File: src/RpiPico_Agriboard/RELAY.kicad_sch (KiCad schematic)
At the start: 7 parts, among them J8 Screw_Terminal_01x03, K2 G5Q-14 DC5, Q10 AP3404

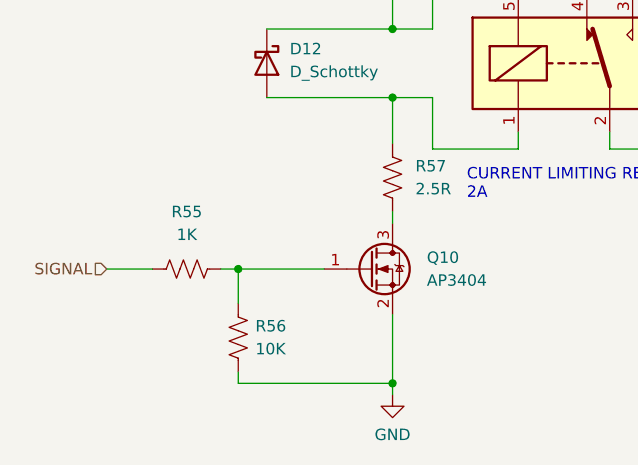
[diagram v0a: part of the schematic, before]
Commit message: power module supply line increase and reupdates on schematic
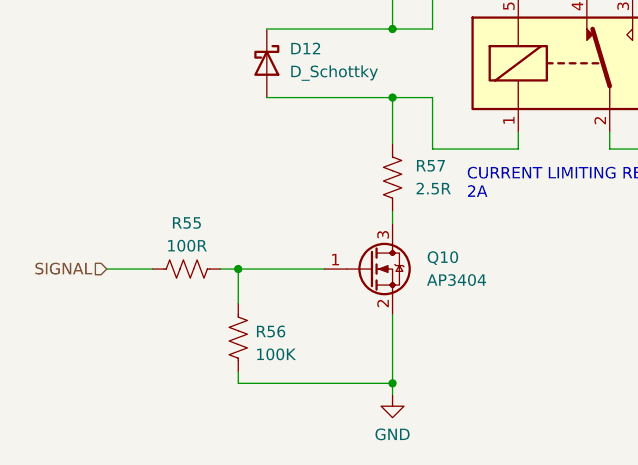
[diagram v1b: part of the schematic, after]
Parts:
- R55: value 1K -> 100R
- R56: value 10K -> 100K
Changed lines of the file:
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@@
   (symbol (lib_id "Device:R_US") (at 97.79 114.3 90) (unit 1)
     (in_bom yes) (on_board yes) (dnp no) (fields_autoplaced)
-    (property "Reference" "R55" (at 97.79 107.95 90)
+    (property "Reference" "R55" (at 97.79 109.22 90)
       (effects (font (size 1.27 1.27)))
     )
-    (property "Value" "1K" (at 97.79 110.49 90)
+    (property "Value" "100R" (at 97.79 111.76 90)
       (effects (font (size 1.27 1.27)))
     )
@@
   (symbol (lib_id "Device:R_US") (at 103.505 121.92 0) (unit 1)
     (in_bom yes) (on_board yes) (dnp no) (fields_autoplaced)
-    (property "Reference" "R56" (at 105.41 120.6499 0)
+    (property "Reference" "R56" (at 105.41 121.285 0)
       (effects (font (size 1.27 1.27)) (justify left))
     )
-    (property "Value" "10K" (at 105.41 123.1899 0)
+    (property "Value" "100K" (at 105.41 123.825 0)
       (effects (font (size 1.27 1.27)) (justify left))
     )

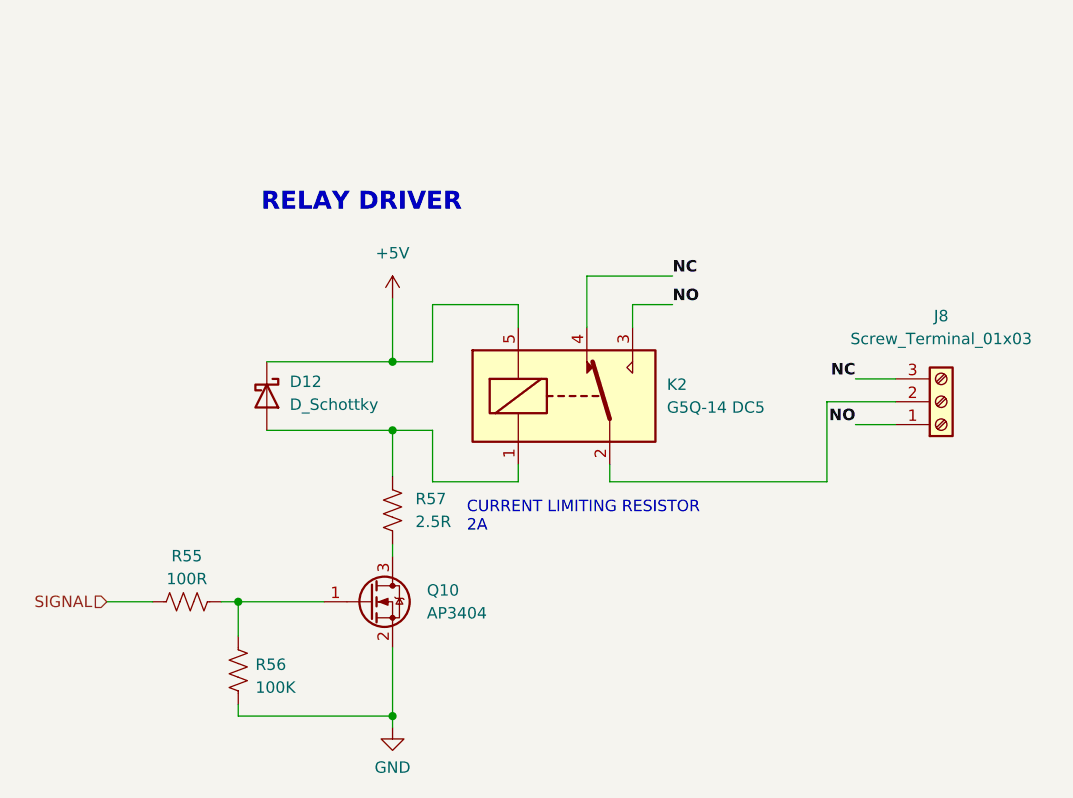
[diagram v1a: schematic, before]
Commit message: complete board update and routing
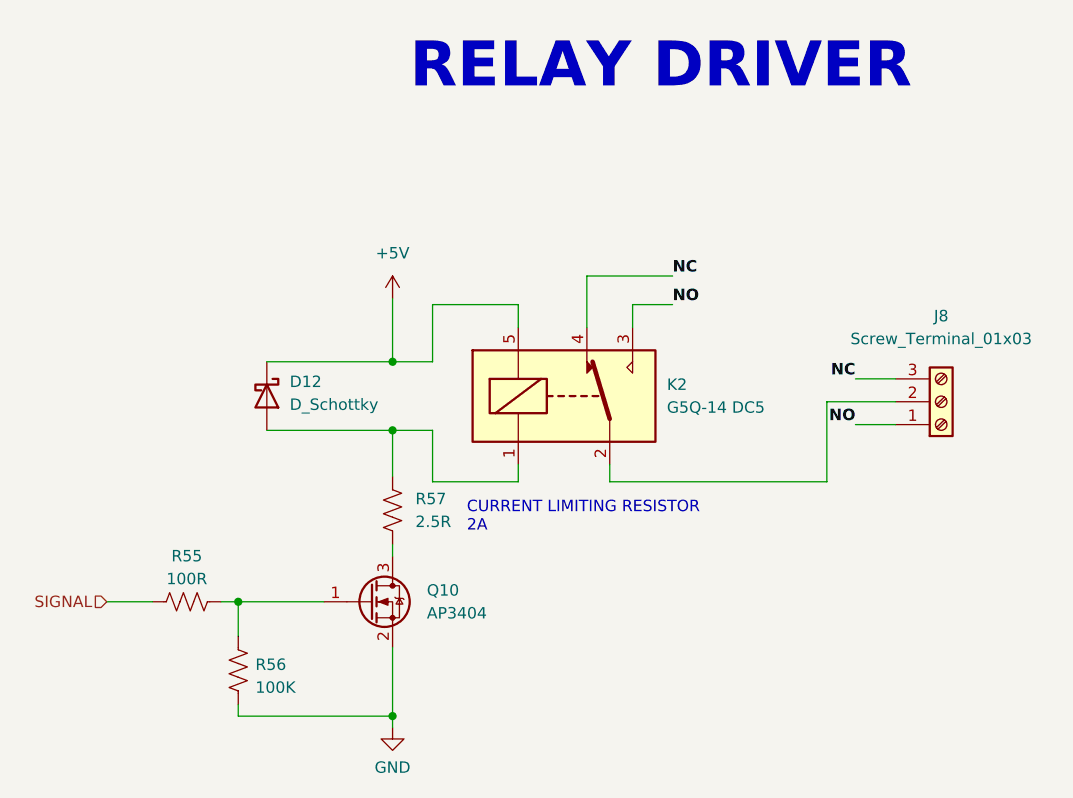
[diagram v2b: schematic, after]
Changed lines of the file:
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@@
     (effects (font (size 1.27 1.27)) (justify left bottom))
   )
-  (text "RELAY DRIVER\n" (at 106.045 71.12 0)
-    (effects (font (size 2 2) (thickness 0.4) bold) (justify left bottom))
+  (text "RELAY DRIVER\n" (at 122.555 57.785 0)
+    (effects (font (face "Agency FB") (size 5 5) (thickness 0.4) bold) (justify left bottom))
   )
   (label "NC" (at 172.085 89.535 180) (fields_autoplaced)
